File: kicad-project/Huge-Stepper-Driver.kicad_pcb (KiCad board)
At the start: 2 copper layers, 99.1 x 61 mm, 102 parts, among them J1 Screw_Terminal_01x02, J13 Conn_01x04_Male, J14 Conn_01x04_Male, J2 USB_C_Receptacle_USB2.0, J21 Motor 1, J3 Conn_02x04_Odd_Even, J4 Conn_01x02_Female, J5 Conn_01x02_Female, J6 Conn_01x02_Female, J7 Conn_01x04_Male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

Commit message: hw: place layout component
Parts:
- added R19: 0, Resistor_SMD:R_0603_1608Metric, F.Cu at (116.9, 95.0)
- L1: footprint Inductor_SMD:L_0603_1608Metric -> HSD:Inductance
- moved J5 164.9 mm to (184.9, 101.4)
- moved J9 155.0 mm to (185.5, 116.4)
- moved C28 152.7 mm to (165.0, 127.8)
- moved C26 148.1 mm to (164.2, 86.1)
- moved J4 139.0 mm to (184.9, 94.1)
- moved J6 133.9 mm to (185.1, 108.8)
- moved C27 122.7 mm to (133.7, 128.2)
- moved H4 111.3 mm to (184.0, 131.0)
- moved Y1 102.5 mm to (158.8, 104.2), turned to 90 degrees
- moved D1 101.7 mm to (118.5, 83.4), turned to -90 degrees
- moved SW2 101.1 mm to (173.4, 103.2)
- moved J3 101.1 mm to (119.3, 123.6), turned to 90 degrees
- moved C25 95.3 mm to (133.7, 86.2)
- moved C20 94.7 mm to (145.6, 111.0), turned to -90 degrees
- moved R16 94.1 mm to (135.3, 114.7), turned to 90 degrees
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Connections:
- C7 pad 1: +5V -> Net-(C7-Pad1)
- R6 pad 1: /Power Management/SW_FB -> unconnected-(R6-Pad1)
- R6 pad 2: GND -> unconnected-(R6-Pad2)
- U2 pad 3: +5V -> Net-(C7-Pad1)
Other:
- board text added: "58x49mm"
- board text removed: "TODO controllare usb"

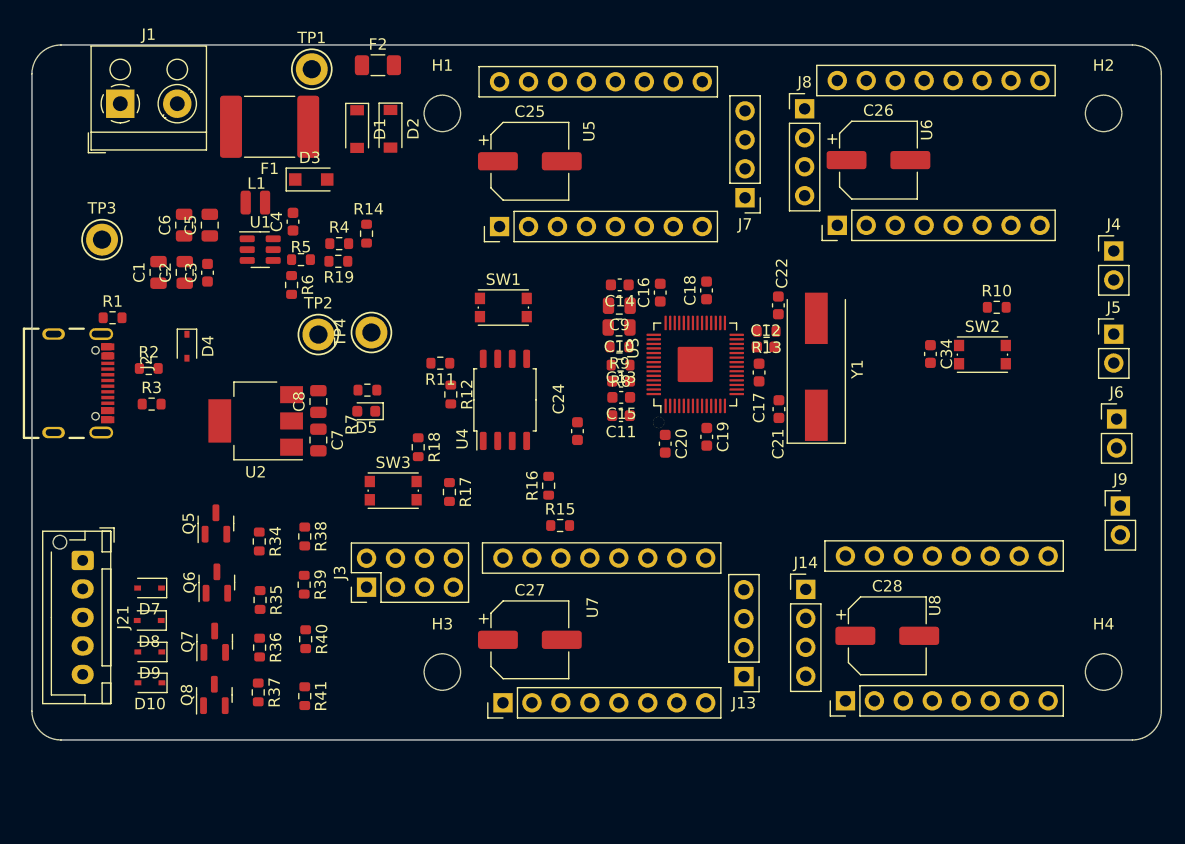
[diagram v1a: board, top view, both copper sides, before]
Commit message: prima versione pcb layout
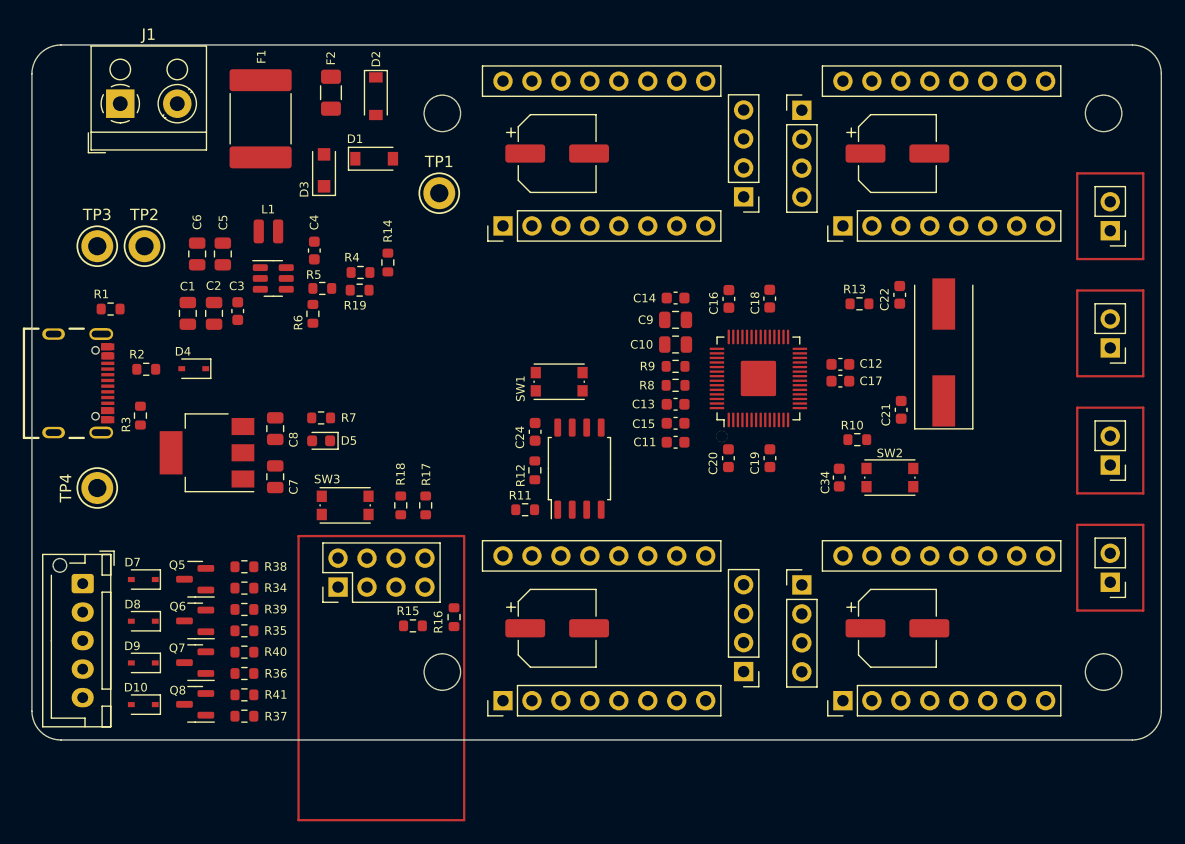
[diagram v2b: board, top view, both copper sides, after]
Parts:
- moved TP4 27.6 mm to (95.7, 114.9)
- moved TP2 17.1 mm to (99.9, 93.6)
- moved R10 16.9 mm to (162.4, 110.6)
- moved R15 15.6 mm to (123.4, 126.9)
- moved TP1 15.6 mm to (125.7, 89.0)
- moved R11 14.9 mm to (133.3, 116.8), turned to 0 degrees
- moved R16 14.2 mm to (127.0, 126.2)
- moved SW2 13.5 mm to (165.3, 113.9)
- moved C34 13.5 mm to (160.8, 113.9)
- moved Y1 11.2 mm to (170.0, 103.0)
- moved C21 10.7 mm to (166.2, 108.0), turned to -90 degrees
- moved C22 10.7 mm to (166.1, 97.9)
- moved R12 9.93 mm to (134.1, 113.3)
- moved U4 8.89 mm to (138.0, 113.2)
- moved R13 8.50 mm to (162.6, 98.7)
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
